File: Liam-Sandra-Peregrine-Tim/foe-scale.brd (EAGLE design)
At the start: 100 x 80 mm, 40 parts, among them U1 LM311, U2 SAMD21E, U3 3.3V_AS1363

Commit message: finished up schematic
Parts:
- U$8: value SDCARD_JACK -> (none); device test:MICRO_SDCARD -> foe-scale:MICRO_SDCARD
- U$9: device test:RED_LED -> foe-scale:RED_LED
- moved U$9 62.4 mm to (-63.5, -1.27)
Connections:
- net N$40 renamed +3.3V
- removed net /SAMPLE-PA01: U1.7
- removed net N$1: U$1.1
- removed net N$11: R3.1
- removed net N$12: R2.2
- removed net N$13: U$3.8
- removed net N$14: U$3.4
- removed net N$15: U$2.+VS
- removed net N$17: C2.2
- removed net N$21: C1.2
- removed net N$22: R7.1
- removed net N$24: R8.2
- removed net N$25: C4.2
- removed net N$26: U1.1
- removed net N$28: C5.2
- removed net N$29: U1.4
- removed net N$30: U1.8
- removed net N$31: U2.26
- removed net N$32: C6.2
- removed net N$33: U$6.3, U$6.4
- removed net N$37: U$6.8
- removed net N$38: U$7.VL
- removed net N$39: U$7.GND, U$7.IVL4
- removed net N$4: U$1.4
- removed net N$41: U$13.GND
- removed net N$42: D1.CH2, U$13.D-
- removed net N$43: D1.CH1, U$13.D+
- removed net N$44: U2.28
- removed net N$47: U$10.A
- removed net N$51: U2.17
- removed net N$52: U2.18
- removed net N$53: U2.19
- removed net N$54: U2.20
- removed net N$55: U2.11
- removed net N$56: U2.12
- removed net N$57: U2.13
- removed net N$58: U2.14
- removed net N$59: U2.30
- removed net N$60: U2.10
- removed net N$61: U2.3
- removed net N$62: U2.9
- removed net N$63: C8.1, R11.1, U3.1
- removed net N$66: C8.2
- removed net N$68: C9.2, U3.6
- removed net N$69: DBG1.VREF
- removed net N$71: U3.4
- removed net N$72: R13.2
- removed net N$73: R13.1
- removed net N$74: DBG1.DGND1, DBG1.DGND2
- removed net N$75: DBG1.SWDIO
- removed net N$76: DBG1.SWDCLK
- removed net N$77: D1.V_N
- removed net N$78: D1.V_P
- removed net N$79: DBG1.NRESET
- removed net N$8: U$2.–VS
- new net /SAMPLE-PA11: U1.7, U2.14
- net +5V: now also C8.1, D1.V_P, R11.1, R2.2, R7.1, U$1.1, U$2.+VS, U$3.8, U$6.8, U$7.VL, U1.8, U3.1; no longer U$9.P+
- net 3.3V: now also C9.2, DBG1.VREF, U$10.A, U$8.VDD, U2.30, U2.9, U3.6; no longer U$8.P4
- net AGND: now also C1.2, C2.2, C4.2, C5.2, R13.2, R3.1, R8.2, U$1.4, U$2.–VS, U$3.4, U$6.3, U$6.4, U$7.GND, U$7.IVL4, U1.1, U1.4; no longer U$9.P-
- net CLK-PA17: now also U$8.CLK, U2.18; no longer U$8.P5
- net CONV-PA10: now also U2.13
- net CS-PA19: now also U$8.CD, U2.20; no longer U$8.P2
- net DGND: now also C6.2, C8.2, D1.V_N, DBG1.DGND1, DBG1.DGND2, R13.1, U$13.GND, U$8.VSS, U2.10, U2.28, U3.4; no longer U$8.P6
- net DI-PA18: now also U$8.CMD, U2.19; no longer U$8.P3
- net DO-PA16: now also U$8.DAT0, U2.17; no longer U$8.P7
- net HYS-PA02: now also U2.3
- net RST: now also DBG1.NRESET, U2.26
- net SCK-PA08: now also U2.11
- net SDO-PA09: now also U2.12
- net SWDCLK: now also DBG1.SWDCLK
- net SWDIO: now also DBG1.SWDIO
- net USB_D+_PA25: now also D1.CH1, U$13.D+
- net USB_D-_PA24: now also D1.CH2, U$13.D-

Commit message: updated layout file
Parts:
- moved U$10 147.9 mm to (91.4, 74.9), turned to 270 degrees
- moved C7 114.7 mm to (96.5, 42.5), turned to 90 degrees
- moved U3 114.6 mm to (49.5, 72.4), turned to 180 degrees
- moved R10 114.4 mm to (50.8, 67.3), turned to 90 degrees
- moved U$12 110.5 mm to (71.1, 25.4), turned to 270 degrees
- moved C6 109.8 mm to (48.3, 67.3), turned to 90 degrees
- moved R12 105.4 mm to (52.1, 77.5), turned to 90 degrees
- moved C8 104.8 mm to (67.3, 27.9), turned to 90 degrees
- moved U$11 99.6 mm to (71.1, 31.8), turned to 90 degrees
- moved U1 91.6 mm to (29.2, 68.6)
- moved R13 86.9 mm to (67.3, 33.0), turned to 90 degrees
- moved C5 84.0 mm to (40.6, 67.3), turned to 90 degrees
- moved R8 80.5 mm to (36.8, 58.4)
- moved R9 79.0 mm to (40.6, 71.1), turned to 90 degrees
- moved C3 76.6 mm to (21.6, 63.5), turned to 180 degrees
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
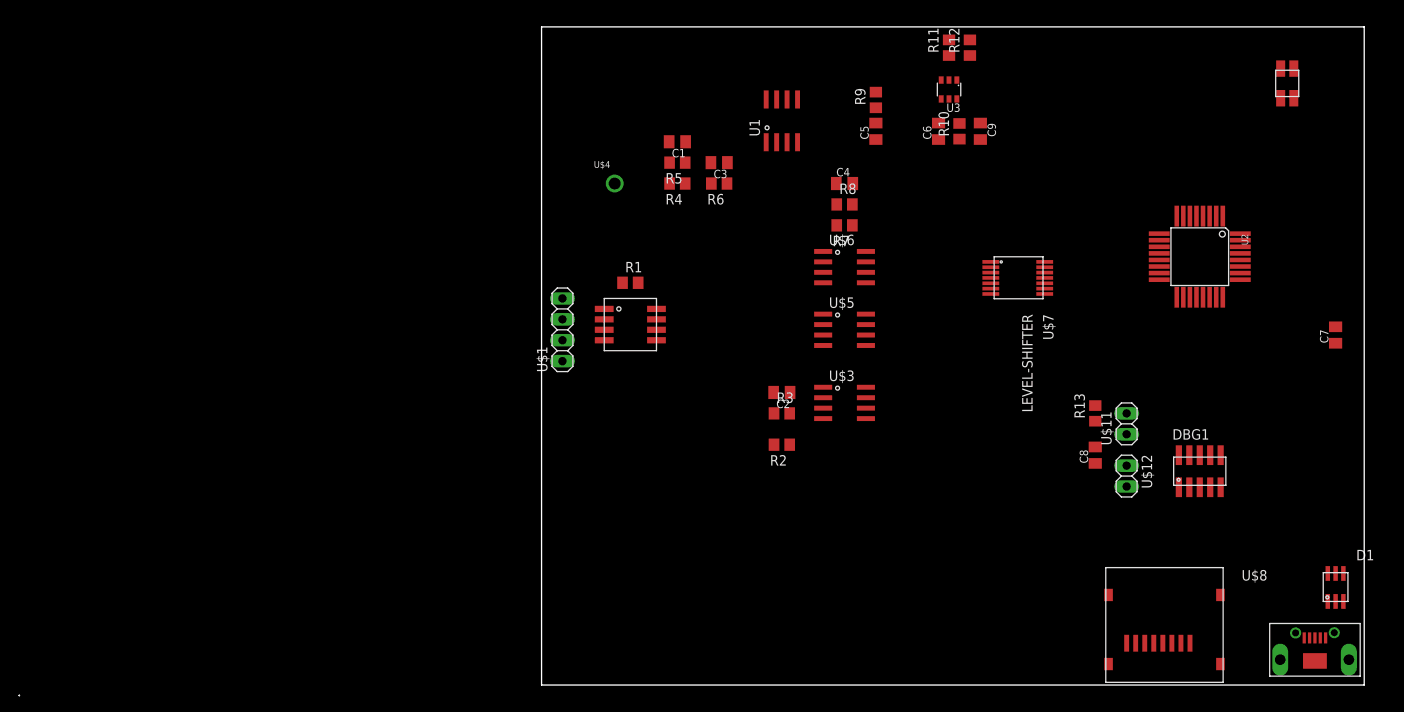
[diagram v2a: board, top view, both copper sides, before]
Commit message: added some labels, consolidated space, moved some parts around to generate dividing plane
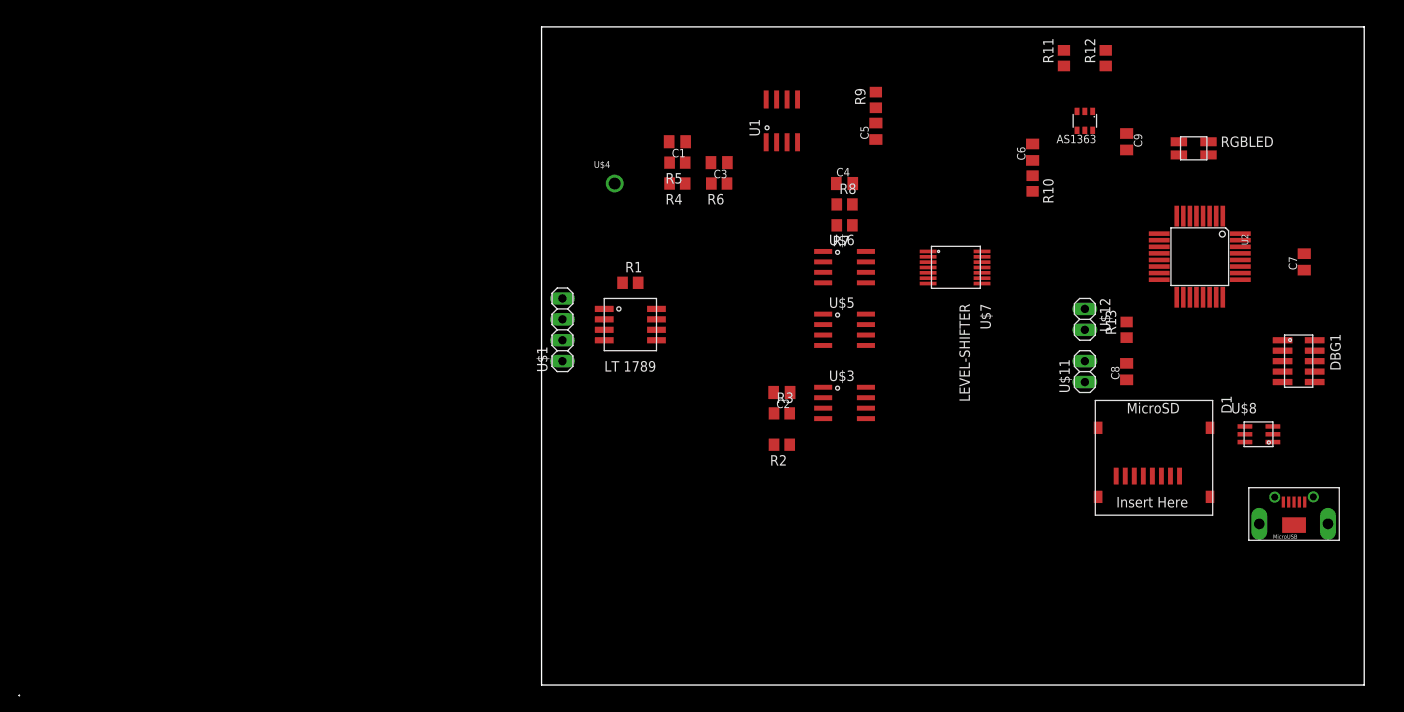
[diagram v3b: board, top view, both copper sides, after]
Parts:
- removed U3: 3.3V_AS1363, foe-scale:SOT23-6
- added AS1363: (no value), foe-scale:SOT23-6
- moved D1 21.7 mm to (88.9, 30.5), turned to 90 degrees
- moved DBG1 21.6 mm to (94.0, 41.9), turned to 270 degrees
- moved U$8 20.4 mm to (69.8, 25.4)
- moved U$12 19.7 mm to (66.0, 44.5)
- moved C9 17.8 mm to (71.1, 66.0)
- moved U$13 16.7 mm to (90.2, 21.6)
- moved R12 16.6 mm to (68.6, 76.2)
- moved U$10 16.6 mm to (77.5, 66.0), turned to 0 degrees
- moved R11 14.0 mm to (63.5, 76.2)
- moved C6 11.7 mm to (59.7, 64.8)
- moved R10 10.9 mm to (59.7, 61.0), turned to 270 degrees
- moved C8 10.9 mm to (71.1, 38.1)
- moved R13 10.9 mm to (71.1, 43.2)
- moved C7 9.67 mm to (92.7, 51.4)
- moved U$11 8.13 mm to (66.0, 38.1)
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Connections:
- net +5V: now also AS1363.1; no longer U3.1
- net 3.3V: now also AS1363.6; no longer U3.6
- net DGND: now also AS1363.4; no longer U3.4
- net N$64: now also AS1363.3; no longer U3.3
- net N$67: now also AS1363.5; no longer U3.5
- net N$70: now also AS1363.2; no longer U3.2
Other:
- board text added: "LT 1789"

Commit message: minor changes
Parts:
- moved DBG1 3.59 mm to (96.5, 44.5)
- moved U2 1.27 mm to (80.0, 53.3)
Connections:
- removed net +3.3V: U$7.VCC
- removed net N$9: R10.2
- net 3.3V: now also R10.2, U$7.VCC
- net SCK-PA08: no longer U$7.IVCC1
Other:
- board size 100 x 80 mm -> 100 x 81.3 mm

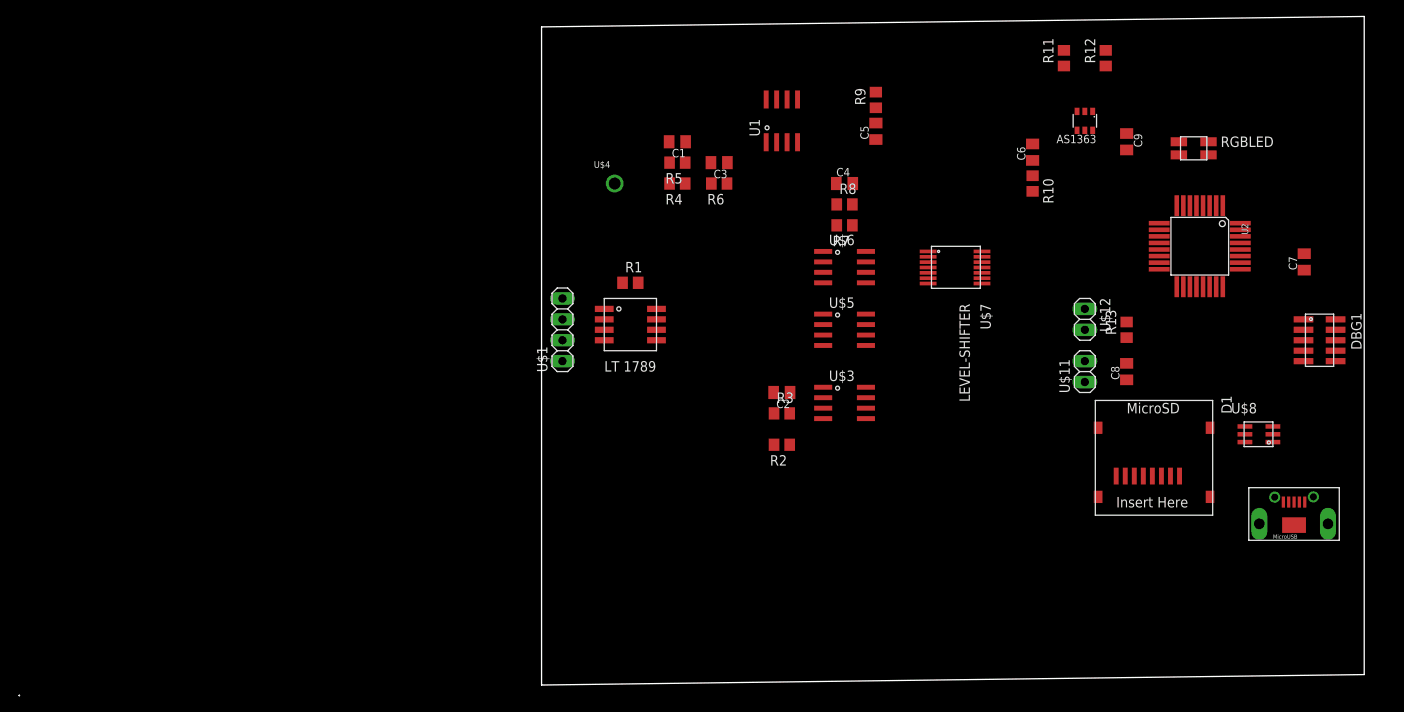
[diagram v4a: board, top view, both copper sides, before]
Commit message: added power and gnd connections
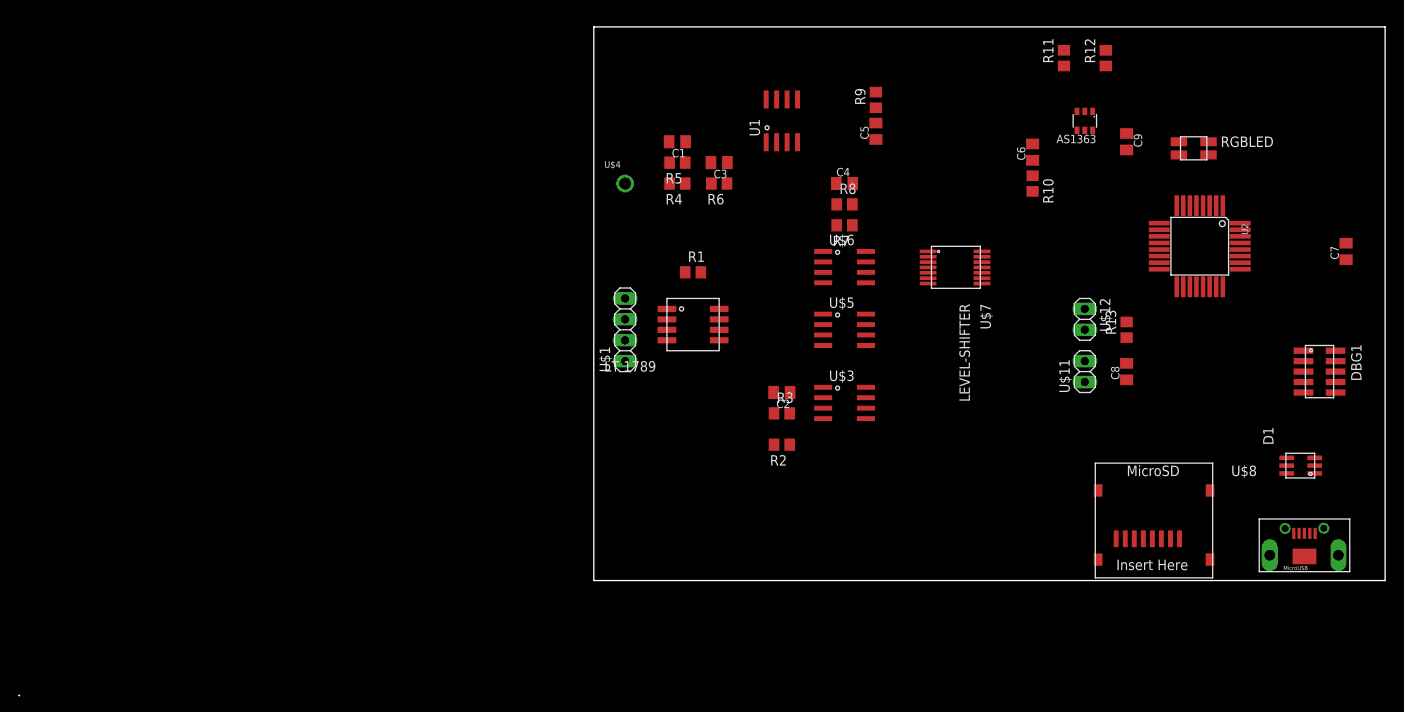
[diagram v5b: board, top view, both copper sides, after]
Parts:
- moved R1 7.73 mm to (18.4, 50.2)
- moved U$1 7.62 mm to (10.2, 43.2)
- moved U$2 7.62 mm to (15.2, 45.7)
- moved U$8 7.62 mm to (69.8, 17.8)
- moved D1 6.35 mm to (94.0, 26.7)
- moved C7 5.24 mm to (97.8, 52.7)
- moved U$13 4.02 mm to (91.4, 17.8)
- moved DBG1 3.81 mm to (96.5, 40.6)
- moved U$4 1.27 mm to (10.2, 61.0)
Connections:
- removed net 3.3V: AS1363.6, C9.2, DBG1.VREF, R10.2, U$10.A, U$7.VCC, U$8.VDD, U2.30, U2.9
- removed net N$46: C7.1
- removed net N$65: R12.1
- new net +3V3: AS1363.6, C9.2, DBG1.VREF, R10.2, R12.1, U$10.A, U$7.VCC, U$8.VDD, U2.30, U2.9
- new net TESTTESTTEST: C4.2
- net AGND: no longer C4.2
- net DGND: now also C7.1
- net SCK-PA08: now also U$7.IVCC1
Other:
- board size 100 x 81.3 mm -> 96.2 x 67.3 mm

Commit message: made a few changes to layout
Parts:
- added R14, R15: 15, resistor:R0805
- added R16: 70, resistor:R0805
- U$11, U$12: value PUSHBTN -> BUTTON_THRU; device foe-scale:1X02 -> foe-scale:PUSHBTN
- moved U$12 36.8 mm to (92.7, 69.8)
- moved C8 33.0 mm to (83.8, 68.6), turned to 0 degrees
- moved U$11 32.1 mm to (92.7, 55.9), turned to 270 degrees
- moved R13 25.0 mm to (83.8, 64.8), turned to 180 degrees
- moved U2 12.0 mm to (73.7, 43.2)
- moved C9 7.73 mm to (63.5, 64.8)
- moved U$10 5.68 mm to (72.4, 63.5), turned to 90 degrees
- moved C7 5.08 mm to (97.8, 47.6)
- moved AS1363 2.54 mm to (66.0, 71.1)
- moved DBG1 1.80 mm to (97.8, 39.4)
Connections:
- new net N$1: R14.1, U2.4
- new net N$4: R15.1, U2.5
- new net N$8: R16.1, U2.6
- net AGND: no longer U$7.GND, U$7.IVL4
- net DGND: now also U$7.GND, U$7.IVL4
- net N$2: now also U$12.4; no longer U$12.2
- net N$3: now also U$11.4; no longer U$11.2
- net N$48: now also R14.2; no longer U2.4
- net N$49: now also R15.2; no longer U2.5
- net N$50: now also R16.2; no longer U2.6

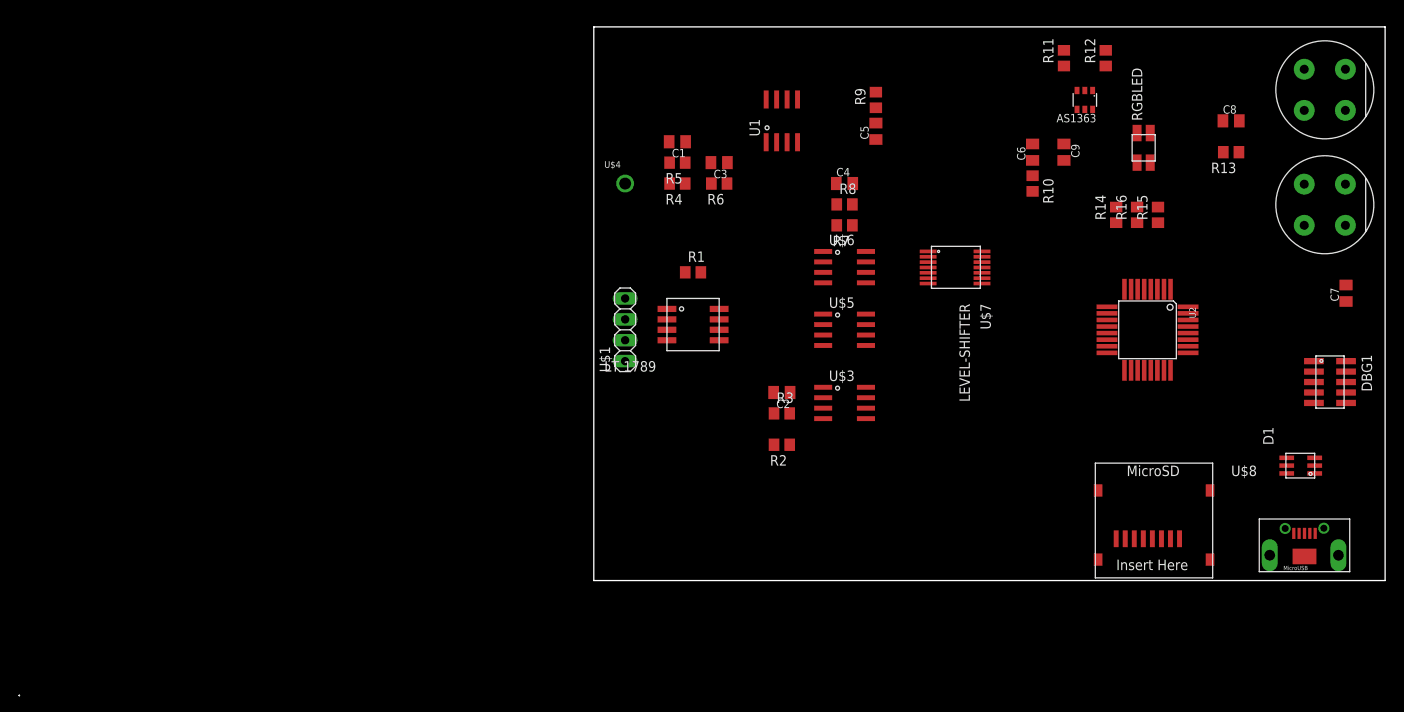
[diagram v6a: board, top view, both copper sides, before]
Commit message: finished up layout. Try to place all of the names and values of th components so that they do not overlap. To do so, use the smash command by typing smash and then clicking on the component. Xs will appear next to the component name and value, and thee will appear on the silk screen. Move them around so that none overlap and so that they are right next to the component that they correspond to. You can change the size of the text in properties if need be.
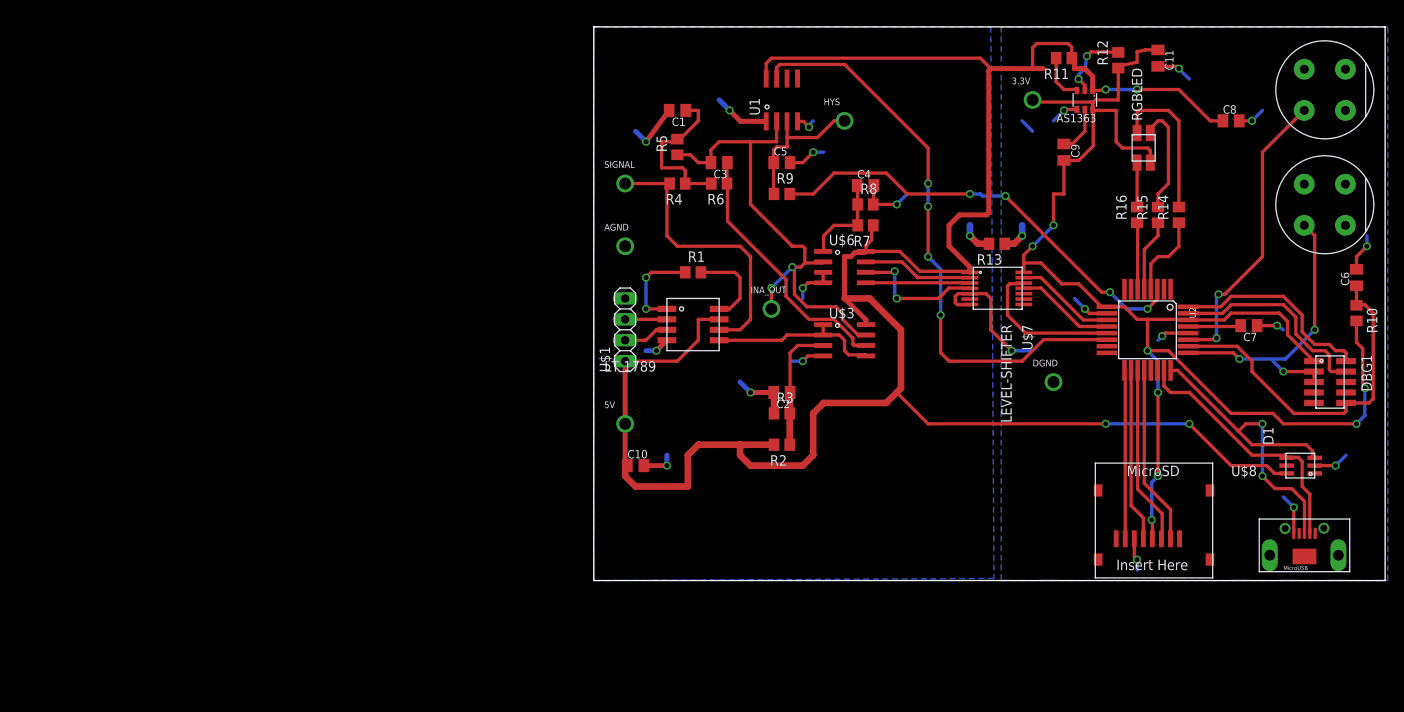
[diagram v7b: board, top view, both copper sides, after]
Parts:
- removed U$5: LMC6482, foe-scale:SOIC8
- removed U$9: RED_LED, foe-scale:RED_LED
- added 3.3V, 5V, AGND, DGND, HYS, INA_OUT: TEST_POINT, foe-scale:TEST_POINT
- added C10, C11: 1uF, rcl:C0805K
- moved R10 42.4 mm to (99.1, 45.2)
- moved C6 42.2 mm to (99.1, 49.5)
- moved R13 30.6 mm to (55.4, 53.6)
- moved R9 16.2 mm to (29.2, 59.7), turned to 0 degrees
- moved C7 12.4 mm to (86.0, 43.7), turned to 180 degrees
- moved C5 12.0 mm to (29.2, 63.5), turned to 0 degrees
- moved R14 7.62 mm to (77.5, 57.1)
- moved U$3 7.62 mm to (36.8, 41.9)
- moved U$7 5.68 mm to (52.1, 50.2)
- moved C1 3.81 mm to (16.5, 69.8)
- moved C4 2.55 mm to (39.4, 60.7)
- moved U1 2.54 mm to (29.2, 71.1)
- moved R7 2.54 mm to (39.4, 55.9)
- moved R8 2.54 mm to (39.4, 58.4)
- moved R5 1.91 mm to (16.5, 65.4), turned to 90 degrees
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- renumbered U$4 to SIGNAL
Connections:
- removed net TESTTESTTEST: C4.2
- net +3V3: now also 3.3V.P$1, C11.1
- net +5V: now also 5V.P$1, C10.1
- net AGND: now also AGND.P$1, C10.2, C4.2
- net DGND: now also C11.2, DGND.P$1
- net N$16: now also U$3.5; no longer U$5.3
- net N$19: now also INA_OUT.P$1, U$3.7; no longer U$5.1
- net N$20: now also U$3.6; no longer U$5.2
- net N$27: now also HYS.P$1
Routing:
- net +5V: track 0.00 -> 275.2 mm, vias 0 -> 4
- net +3V3: track 0.00 -> 172.2 mm, vias 0 -> 8
- net /SAMPLE-PA11: track 0.00 -> 71.4 mm, vias 0 -> 4
- net DGND: track 0.00 -> 70.8 mm, vias 0 -> 13
- net N$19: track 0.00 -> 59.9 mm, vias 0 -> 2
- net AGND: track 0.00 -> 55.2 mm, vias 0 -> 11
- net HYS-PA02: track 0.00 -> 54.6 mm, vias 0 -> 4
- net RST: track 0.00 -> 43.2 mm
- net USB_D+_PA25: track 0.00 -> 42.2 mm, vias 0 -> 2
- net N$2: track 0.00 -> 36.1 mm, vias 0 -> 2
- net N$7: track 0.00 -> 35.1 mm
- net N$20: track 0.00 -> 31.9 mm
- net USB_D-_PA24: track 0.00 -> 31.7 mm
- net N$3: track 0.00 -> 30.4 mm, vias 0 -> 2
- net SWDCLK: track 0.00 -> 25.2 mm
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- added copper zone on layer 16, net AGND
- added copper zone on layer 16, net DGND
